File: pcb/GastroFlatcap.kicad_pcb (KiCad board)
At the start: 2 copper layers, 8 parts, among them J1 INPUT 12V, J2 LED, J3 SERVO, Q1 IRLZ44N

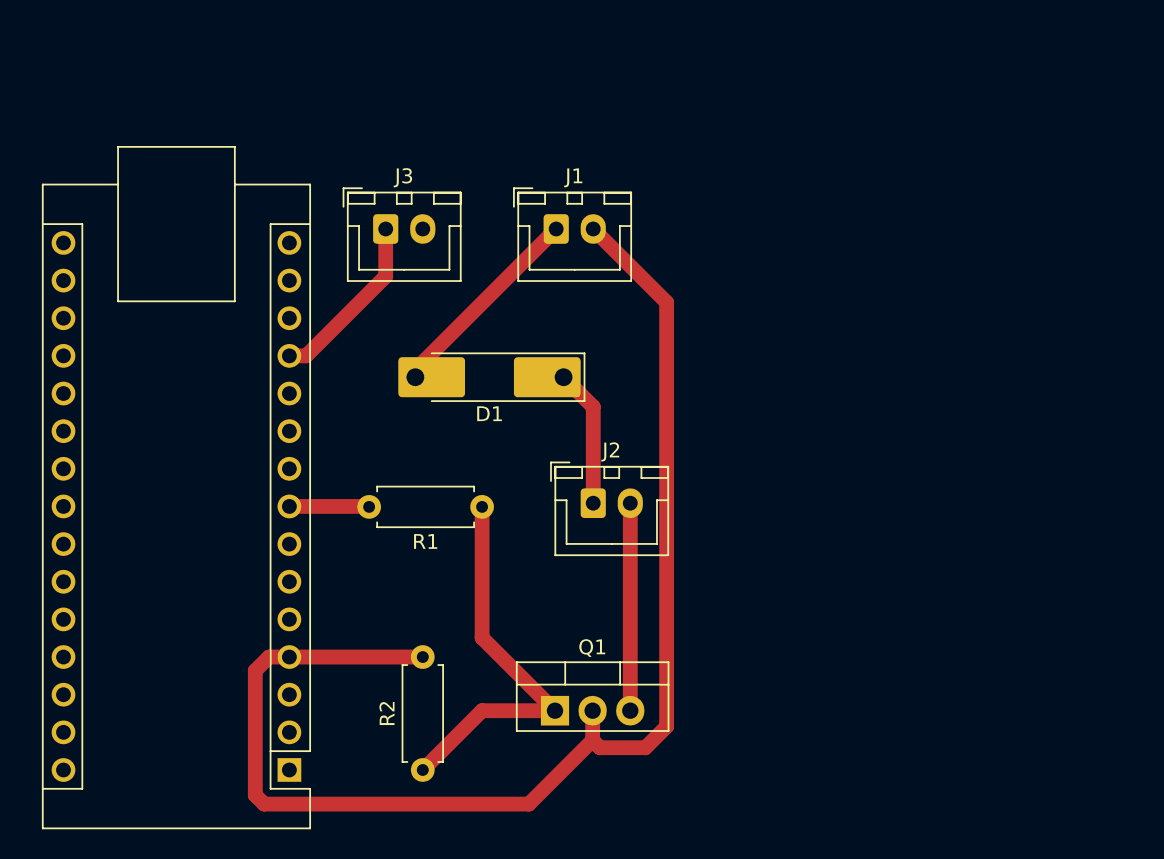
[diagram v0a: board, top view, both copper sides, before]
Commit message: Changed microcontroller to ESP32 S3, merged flatcap with focuser
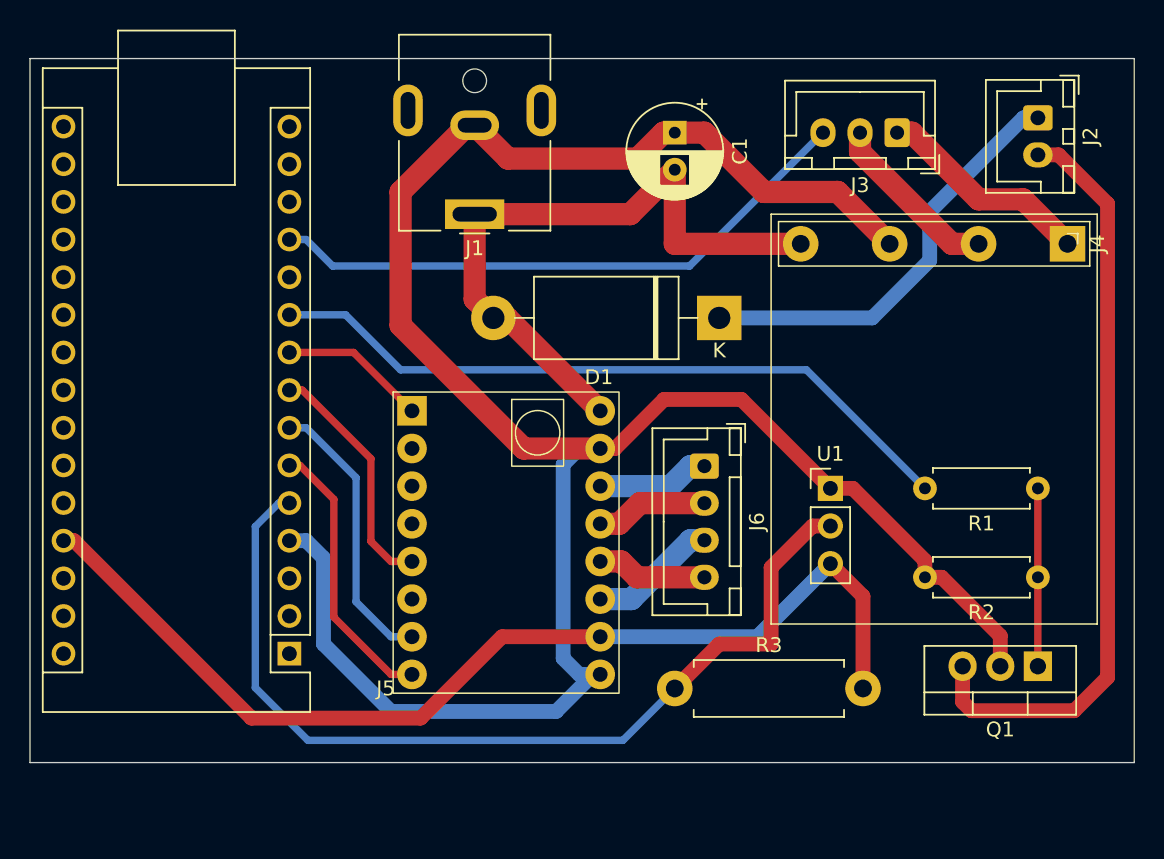
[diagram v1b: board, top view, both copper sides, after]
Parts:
- added C1: 470uF, Capacitor_THT:CP_Radial_D6.3mm_P2.50mm, F.Cu at (76.0, 27.0)
- added J4: 5V_REG, Custom:PinHeader_1x04_P6.00mm_Vertical, F.Cu at (102.5, 34.5)
- added J5: TMC2209, Custom:Pin_Header_02x08_6_spaces_2,50mm, F.Cu at (57.0, 44.5)
- added J6: MTR, Connector_JST:JST_XH_B4B-XH-A_1x04_P2.50mm_Vertical, F.Cu at (78.0, 49.5)
- added R3: 4k7, Resistor_THT:R_Axial_DIN0411_L9.9mm_D3.6mm_P12.70mm_Horizontal, F.Cu at (76.0, 64.5)
- added U1: DS18B20, Connector_PinHeader_2.54mm:PinHeader_1x03_P2.54mm_Vertical, F.Cu at (86.5, 51.0)
- A1: value Arduino_Nano_Every -> Arduino Nano
- D1: value D_Schottky -> SR5100; footprint Diode_SMD:D_MELF-RM10_Universal_Handsoldering -> Diode_THT:D_DO-27_P15.24mm_Horizontal
- J1: value INPUT 12V -> 12V; footprint Connector_JST:JST_XH_B2B-XH-A_1x02_P2.50mm_Vertical -> Connector_BarrelJack:BarrelJack_CUI_PJ-063AH_Horizontal
- J3: footprint Connector_JST:JST_XH_B2B-XH-A_1x02_P2.50mm_Vertical -> Connector_JST:JST_XH_B3B-XH-A_1x03_P2.50mm_Vertical
- moved R2 43.5 mm to (100.5, 57.0), turned to 180 degrees
- moved J2 39.7 mm to (100.5, 26.0), turned to -90 degrees
- moved R1 37.5 mm to (100.5, 51.0)
- moved J3 35.1 mm to (91.0, 27.0), turned to 180 degrees
- moved Q1 32.7 mm to (100.5, 63.0), turned to 180 degrees
- moved D1 16.0 mm to (79.0, 39.5)
- moved A1 7.85 mm to (50.0, 62.1)
- moved J1 5.59 mm to (62.5, 32.5), turned to 180 degrees
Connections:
- A1 pad 10: unconnected-(A1-D7-Pad10) -> Net-(A1-D7)
- A1 pad 12: Net-(A1-D9) -> Net-(A1-D10)
- A1 pad 13: unconnected-(A1-D10-Pad13) -> Net-(A1-D10)
- A1 pad 5: unconnected-(A1-D2-Pad5) -> Net-(A1-D2)
- A1 pad 6: unconnected-(A1-D3-Pad6) -> Net-(A1-D3)
- A1 pad 7: unconnected-(A1-D4-Pad7) -> Net-(A1-D4)
- A1 pad 9: unconnected-(A1-D6-Pad9) -> Net-(A1-D6)
- J3 pad 1: Net-(A1-D9) -> Net-(J3-Pin_1)
- J3 pad 2: unconnected-(J3-Pin_2-Pad2) -> Net-(J3-Pin_2)
- R1 pad 2: Net-(A1-D5) -> Net-(A1-D7)
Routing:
- net Earth: track 88.3 -> 152.4 mm
- net Net-(A1-D2): track 0.00 -> 63.1 mm
- net Net-(A1-D7): track 0.00 -> 47.7 mm
- net (no net): track 0.00 -> 43.4 mm
- net Net-(A1-D10): track 0.00 -> 40.5 mm
- net Net-(J2-Pin_2): track 14.0 -> 51.4 mm
- net Net-(D1-A): track 13.9 -> 45.6 mm
- net Net-(J5-Pin_15): track 0.00 -> 26.9 mm
- net Net-(D1-K): track 9.33 -> 29.0 mm
- net Net-(A1-D4): track 0.00 -> 19.0 mm
- net Net-(A1-D3): track 0.00 -> 18.8 mm
- net Net-(J3-Pin_1): track 0.00 -> 14.6 mm
- net Net-(Q1-G): track 26.4 -> 12.0 mm
- net Net-(A1-D9): track 11.9 -> 0.00 mm
- net Net-(J3-Pin_2): track 0.00 -> 11.9 mm
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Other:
- board outline added: 74.5 x 47.5 mm
